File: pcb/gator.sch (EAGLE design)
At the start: 89 parts, among them J2 POWER_JACKPTH, X1 USB-A-S, Y1 12MHz

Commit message: Added tons of decoupling capacitors
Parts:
- added C20: 10u, SparkFun-Passives:CAP0603-CAP
- added C23, C32, C33, C34, C35, C36, C37, C38, C39, C40, C41, C42, C43, C44: 100n, SparkFun-Passives:CAP0603-CAP
- added U$4: GATOR_HEAD, gator:GATOR_HEAD
- C13, C16, C30, C4, C9: value 2.2u -> 10u
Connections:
- net +3V3: now also C20.2, C41.1, C42.1, C43.1, C44.1
- net GND: now also C20.1, C23.2, C32.2, C33.2, C34.2, C35.2, C36.2, C37.2, C38.2, C39.2, C40.2, C41.2, C42.2, C43.2, C44.2, U$4.L, U$4.R
- net VCCINT: now also C23.1, C32.1, C40.1
- net VCCIO: now also C33.1, C34.1, C35.1, C36.1, C37.1, C38.1, C39.1
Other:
- moved on the sheet: C12, C13, C15, C16, C17, C8, C9, NCP565ST12T3G

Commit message: Added Fusion DRC and CAM settings; added SD SCLK pulldown; added large power supply caps
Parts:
- added C45, C46, C47, C48: 100u, SparkFun-Passives:CAP_POLPTH1
- added C49: 100n, SparkFun-Passives:CAP0603-CAP
- added R38: 10K, SparkFun-Passives:RESISTOR0603-RES
- C6: value 2.2u -> 10u
- R14, R15: value 110 -> 120
- R19: value 5K6 -> 4K7
- R20: value 10K -> 4K7
- R29: value 50 -> 51
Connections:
- net +3V3: now also C45.+
- net GND: now also C45.-, C46.-, C47.-, C48.-, C49.2, R38.1
- net HDMI_DETECT: now also C49.1
- net SD_CLK: now also R38.2
- net V+: now also C47.+, C48.+
- net VCCINT: now also C46.+
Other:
- note added: "Place C20 near SD socket to minimize hotplug ripple"
- moved on the sheet: C20
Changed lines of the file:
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@@
 <part name="P+1" library="supply1" deviceset="V+" device=""/>
 <part name="SUPPLY8" library="supply2" deviceset="GND" device=""/>
-<part name="C6" library="SparkFun-Passives" deviceset="CAP" device="0603-CAP" value="2.2u"/>
+<part name="C6" library="SparkFun-Passives" deviceset="CAP" device="0603-CAP" value="10u"/>
 <part name="P+4" library="supply1" deviceset="V+" device=""/>
 <part name="D1" library="SparkFun-DiscreteSemi" deviceset="DIODE" device="PTH" value="RPROT"/>
@@
 <part name="+3V8" library="supply1" deviceset="+3V3" device=""/>
 <part name="+3V9" library="supply1" deviceset="+3V3" device=""/>
-<part name="R14" library="SparkFun-Passives" deviceset="RESISTOR" device="0603-RES" value="110"/>
-<part name="R15" library="SparkFun-Passives" deviceset="RESISTOR" device="0603-RES" value="110"/>
+<part name="R14" library="SparkFun-Passives" deviceset="RESISTOR" device="0603-RES" value="120"/>
+<part name="R15" library="SparkFun-Passives" deviceset="RESISTOR" device="0603-RES" value="120"/>
 <part name="+3V10" library="supply1" deviceset="+3V3" device=""/>
 <part name="C21" library="SparkFun-Passives" deviceset="CAP" device="0603-CAP" value="10u"/>
@@
 <part name="P+12" library="supply1" deviceset="V+" device=""/>
 <part name="SUPPLY24" library="supply2" deviceset="GND" device=""/>
-<part name="R19" library="SparkFun-Passives" deviceset="RESISTOR" device="0603-RES" value="5K6"/>
-<part name="R20" library="SparkFun-Passives" deviceset="RESISTOR" device="0603-RES" value="10K"/>
+<part name="R19" library="SparkFun-Passives" deviceset="RESISTOR" device="0603-RES" value="4K7"/>
+<part name="R20" library="SparkFun-Passives" deviceset="RESISTOR" device="0603-RES" value="4K7"/>
 <part name="U$2" library="gator" deviceset="HDMI_A" device=""/>
 <part name="SDRAM" library="gator" deviceset="MT48LC16M16A2P" device=""/>
@@
 <part name="X1" library="SparkFun-Connectors" deviceset="USB" device="-A-S"/>
 <part name="VCC11" library="supply1" deviceset="VCCIO" device=""/>
-<part name="R29" library="SparkFun-Passives" deviceset="RESISTOR" device="0603-RES" value="50"/>
+<part name="R29" library="SparkFun-Passives" deviceset="RESISTOR" device="0603-RES" value="51"/>
 <part name="R30" library="SparkFun-Passives" deviceset="RESISTOR" device="0603-RES" value="4K7"/>
 <part name="R31" library="SparkFun-Passives" deviceset="RESISTOR" device="0603-RES" value="4K7"/>
@@
 <part name="C43" library="SparkFun-Passives" deviceset="CAP" device="0603-CAP" value="100n"/>
 <part name="C44" library="SparkFun-Passives" deviceset="CAP" device="0603-CAP" value="100n"/>
+<part name="C45" library="SparkFun-Passives" deviceset="CAP_POL" device="PTH1" value="100u"/>
+<part name="C46" library="SparkFun-Passives" deviceset="CAP_POL" device="PTH1" value="100u"/>
+<part name="C47" library="SparkFun-Passives" deviceset="CAP_POL" device="PTH1" value="100u"/>
+<part name="C48" library="SparkFun-Passives" deviceset="CAP_POL" device="PTH1" value="100u"/>
+<part name="C49" library="SparkFun-Passives" deviceset="CAP" device="0603-CAP" value="100n"/>
+<part name="R38" library="SparkFun-Passives" deviceset="RESISTOR" device="0603-RES" value="10K"/>
 </parts>
 <sheets>
@@
 <plain>
 <text x="-322.58" y="116.84" size="1.778" layer="91">PLL: M=6, N=168, P=2, Q=7</text>
+<text x="-398.78" y="327.66" size="1.778" layer="91">Place C20 near SD socket
+to minimize hotplug ripple</text>
 </plain>
 <instances>
@@
 <instance part="SUPPLY31" gate="GND" x="-261.62" y="383.54"/>
 <instance part="SUPPLY32" gate="GND" x="-276.86" y="383.54"/>
-<instance part="C20" gate="G$1" x="-370.84" y="322.58" rot="R180"/>
+<instance part="C20" gate="G$1" x="-378.46" y="322.58" rot="R180"/>
 <instance part="C23" gate="G$1" x="33.02" y="431.8"/>
 <instance part="C32" gate="G$1" x="43.18" y="431.8"/>
@@
 <instance part="C43" gate="G$1" x="-101.6" y="386.08"/>
 <instance part="C44" gate="G$1" x="-93.98" y="386.08"/>
+<instance part="C45" gate="G$1" x="-83.82" y="388.62"/>
+<instance part="C46" gate="G$1" x="63.5" y="434.34"/>
+<instance part="C47" gate="G$1" x="-309.88" y="393.7"/>
+<instance part="C48" gate="G$1" x="-299.72" y="393.7"/>
+<instance part="C49" gate="G$1" x="-132.08" y="38.1"/>
+<instance part="R38" gate="G$1" x="-370.84" y="309.88" rot="R90"/>
 </instances>
 <busses>
@@
 <junction x="-363.22" y="304.8"/>
 <pinref part="C20" gate="G$1" pin="1"/>
-<wire x1="-370.84" y1="317.5" x2="-363.22" y2="317.5" width="0.1524" layer="91"/>
+<wire x1="-378.46" y1="317.5" x2="-363.22" y2="317.5" width="0.1524" layer="91"/>
 <junction x="-363.22" y="317.5"/>
+<pinref part="R38" gate="G$1" pin="1"/>
+<wire x1="-370.84" y1="304.8" x2="-363.22" y2="304.8" width="0.1524" layer="91"/>
 </segment>
 <segment>
@@
 <wire x1="-320.04" y1="388.62" x2="-347.98" y2="388.62" width="0.1524" layer="91"/>
 <junction x="-347.98" y="388.62"/>
+<pinref part="C47" gate="G$1" pin="-"/>
+<wire x1="-309.88" y1="388.62" x2="-320.04" y2="388.62" width="0.1524" layer="91"/>
+<junction x="-320.04" y="388.62"/>
+<pinref part="C48" gate="G$1" pin="-"/>
+<wire x1="-299.72" y1="388.62" x2="-309.88" y2="388.62" width="0.1524" layer="91"/>
+<junction x="-309.88" y="388.62"/>
 </segment>
 <segment>
@@
 <wire x1="-93.98" y1="383.54" x2="-101.6" y2="383.54" width="0.1524" layer="91"/>
 <junction x="-101.6" y="383.54"/>
+<pinref part="C45" gate="G$1" pin="-"/>
+<wire x1="-83.82" y1="383.54" x2="-93.98" y2="383.54" width="0.1524" layer="91"/>
+<junction x="-93.98" y="383.54"/>
 </segment>
 <segment>
@@
 <wire x1="53.34" y1="429.26" x2="43.18" y2="429.26" width="0.1524" layer="91"/>
 <junction x="43.18" y="429.26"/>
+<pinref part="C46" gate="G$1" pin="-"/>
+<wire x1="63.5" y1="429.26" x2="53.34" y2="429.26" width="0.1524" layer="91"/>
+<junction x="53.34" y="429.26"/>
 </segment>
 <segment>
@@
 <pinref part="U$2" gate="G$1" pin="TMDS_D1_SHLD"/>
 <pinref part="U$2" gate="G$1" pin="TMDS_D2_SHLD"/>
+<pinref part="C49" gate="G$1" pin="2"/>
+<wire x1="-132.08" y1="35.56" x2="-132.08" y2="33.02" width="0.1524" layer="91"/>
+<wire x1="-132.08" y1="33.02" x2="-121.92" y2="33.02" width="0.1524" layer="91"/>
+<junction x="-121.92" y="33.02"/>
 </segment>
 <segment>
@@
 <wire x1="-363.22" y1="325.12" x2="-363.22" y2="327.66" width="0.1524" layer="91"/>
 <pinref part="C20" gate="G$1" pin="2"/>
-<wire x1="-370.84" y1="325.12" x2="-363.22" y2="325.12" width="0.1524" layer="91"/>
+<wire x1="-378.46" y1="325.12" x2="-363.22" y2="325.12" width="0.1524" layer="91"/>
 <junction x="-363.22" y="325.12"/>
 </segment>
@@
 <wire x1="-101.6" y1="391.16" x2="-93.98" y2="391.16" width="0.1524" layer="91"/>
 <junction x="-101.6" y="391.16"/>
+<pinref part="C45" gate="G$1" pin="+"/>
+<wire x1="-93.98" y1="391.16" x2="-83.82" y2="391.16" width="0.1524" layer="91"/>
+<junction x="-93.98" y="391.16"/>
 </segment>
 <segment>
@@
 <segment>
 <pinref part="MICROSD" gate="G$1" pin="SCK"/>
-<wire x1="-345.44" y1="322.58" x2="-347.98" y2="322.58" width="0.1524" layer="91"/>
 <label x="-355.6" y="322.58" size="1.778" layer="95"/>
+<pinref part="R38" gate="G$1" pin="2"/>
+<wire x1="-345.44" y1="322.58" x2="-370.84" y2="322.58" width="0.1524" layer="91"/>
+<wire x1="-370.84" y1="322.58" x2="-370.84" y2="314.96" width="0.1524" layer="91"/>
 </segment>
 <segment>
@@
 <wire x1="-335.28" y1="396.24" x2="-320.04" y2="396.24" width="0.1524" layer="91"/>
 <junction x="-320.04" y="396.24"/>
+<pinref part="C47" gate="G$1" pin="+"/>
+<wire x1="-320.04" y1="396.24" x2="-309.88" y2="396.24" width="0.1524" layer="91"/>
+<pinref part="C48" gate="G$1" pin="+"/>
+<wire x1="-309.88" y1="396.24" x2="-299.72" y2="396.24" width="0.1524" layer="91"/>
+<junction x="-309.88" y="396.24"/>
 </segment>
 <segment>
@@
 <wire x1="53.34" y1="439.42" x2="53.34" y2="436.88" width="0.1524" layer="91"/>
 <junction x="43.18" y="439.42"/>
+<pinref part="C46" gate="G$1" pin="+"/>
+<wire x1="63.5" y1="436.88" x2="63.5" y2="439.42" width="0.1524" layer="91"/>
+<wire x1="63.5" y1="439.42" x2="53.34" y2="439.42" width="0.1524" layer="91"/>
+<junction x="53.34" y="439.42"/>
 </segment>
 <segment>
@@
 <junction x="-121.92" y="43.18"/>
 <label x="-142.24" y="43.18" size="1.778" layer="95"/>
+<pinref part="C49" gate="G$1" pin="1"/>
 </segment>
 <segment>
@@
 </schematic>
 </drawing>
+<compatibility>
+<note version="6.3" minversion="6.2.2" severity="warning">
+Since Version 6.2.2 text objects can contain more than one line,
+which will not be processed correctly with this version.
+</note>
+</compatibility>
 </eagle>

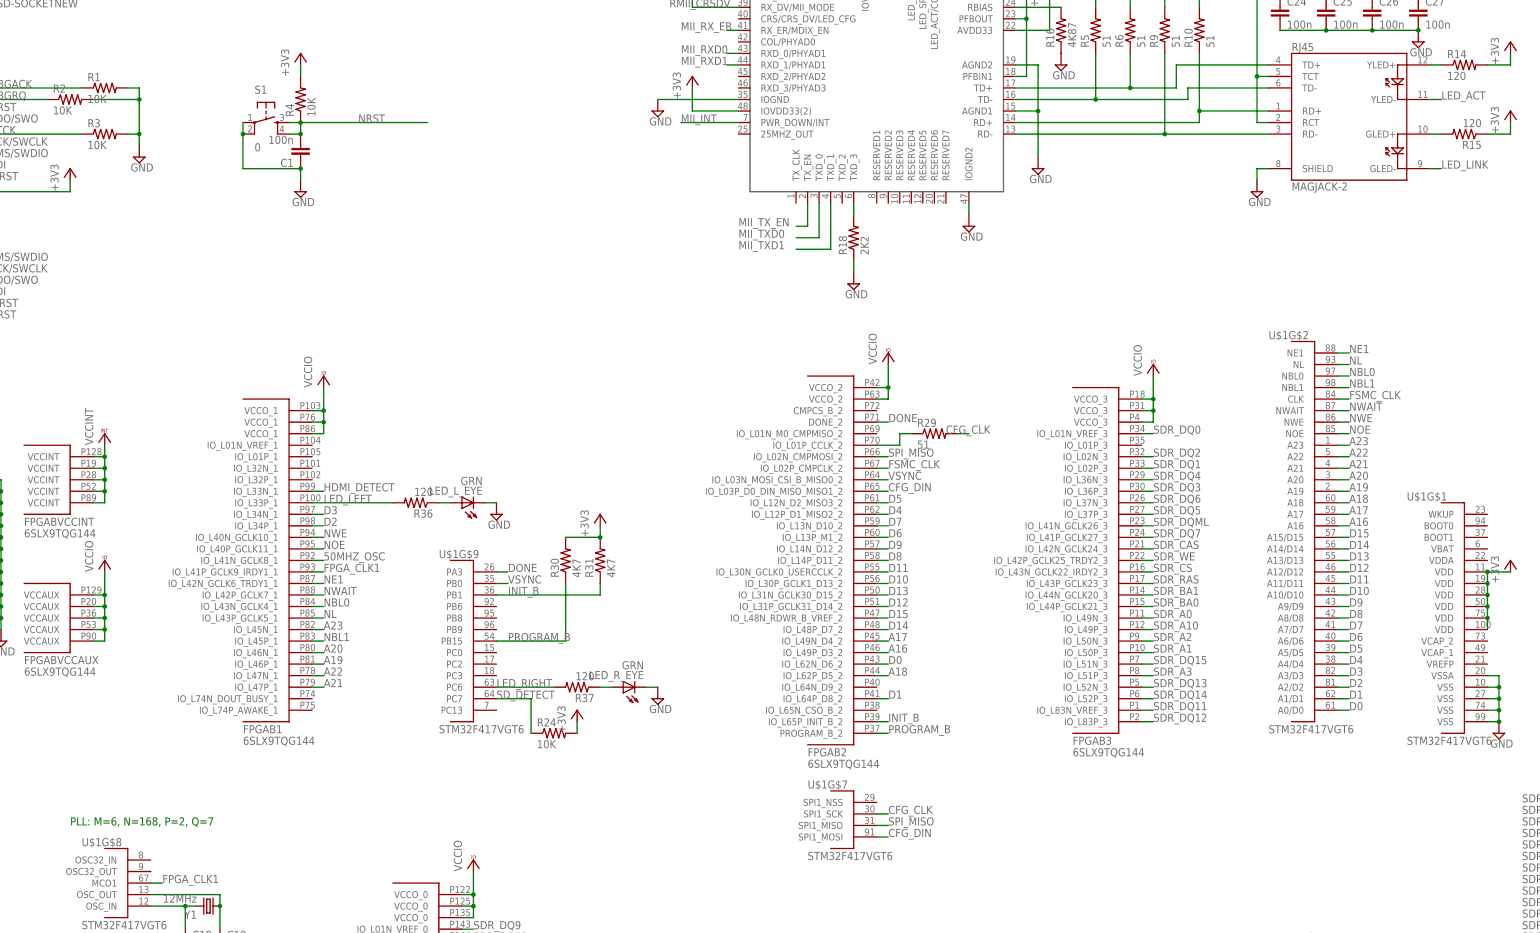
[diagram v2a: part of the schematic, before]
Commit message: Renamed some parts for clarity
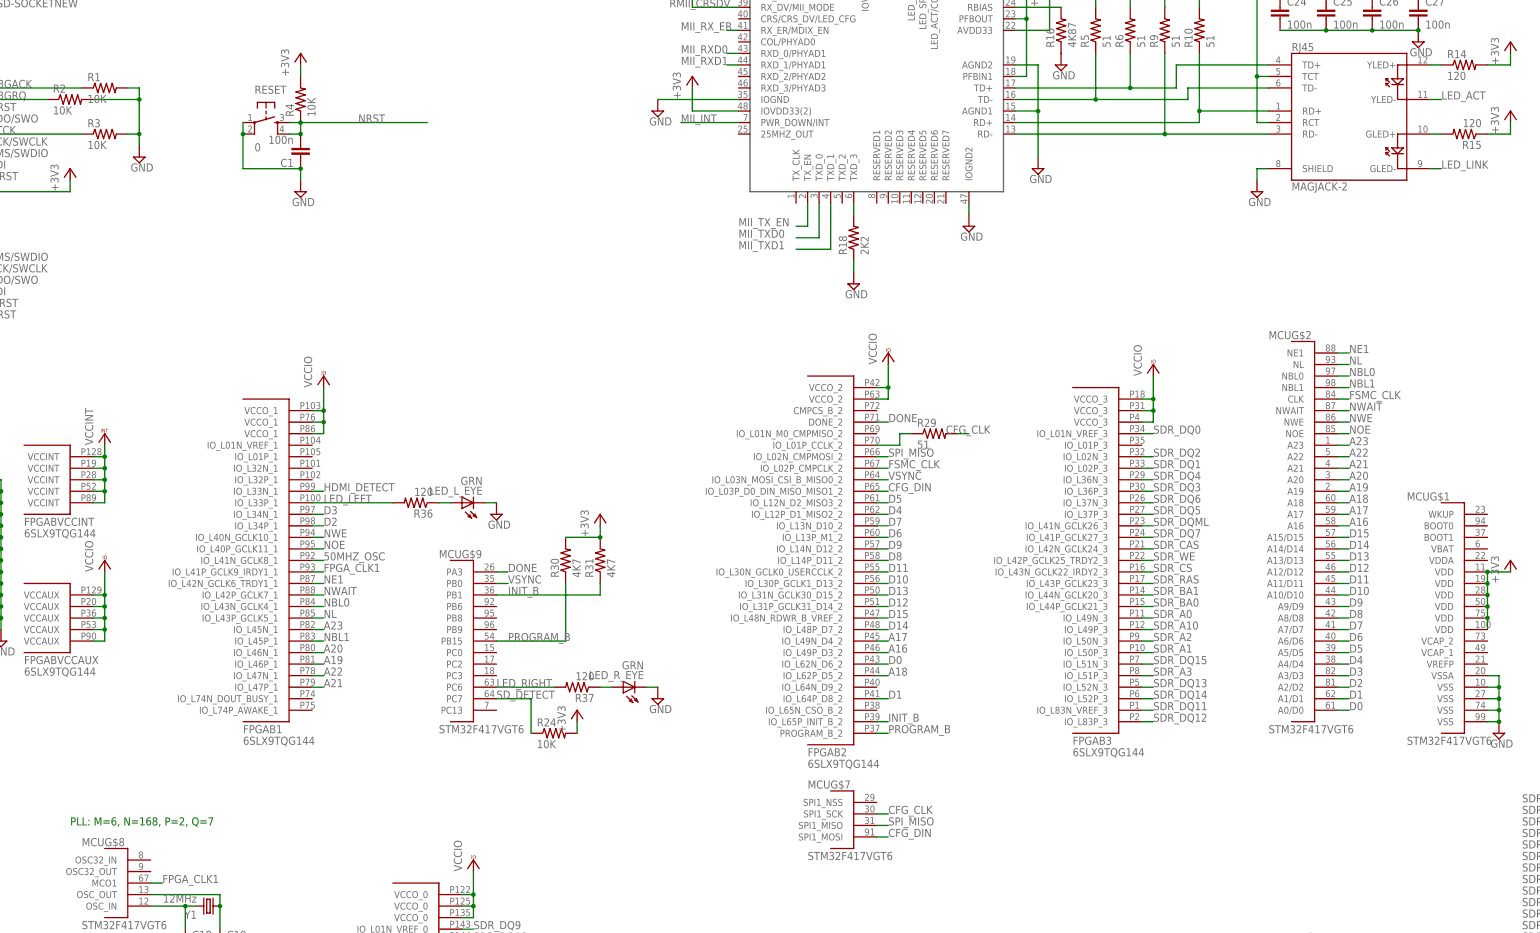
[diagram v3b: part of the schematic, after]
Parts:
- renumbered S1 to RESET, U$1 to MCU

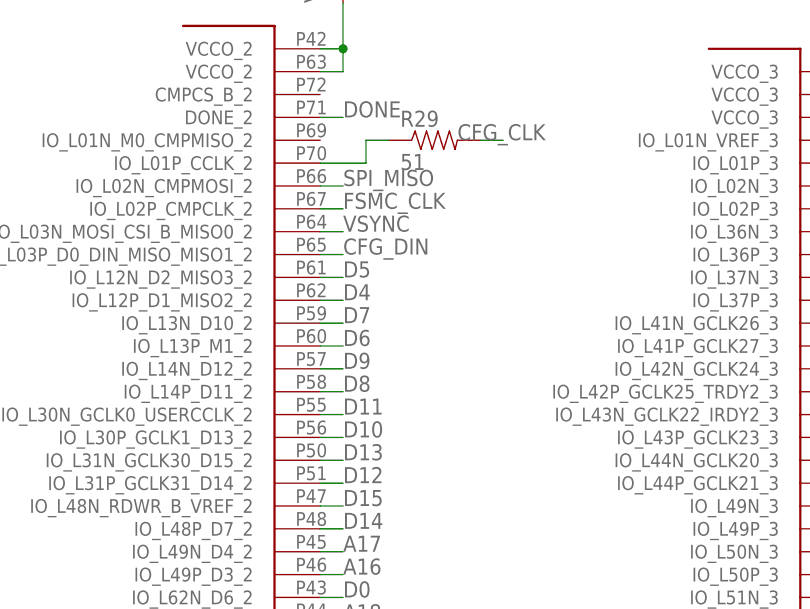
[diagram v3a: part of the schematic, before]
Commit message: Moved FSMC_CLK to a clock input on the FPGA
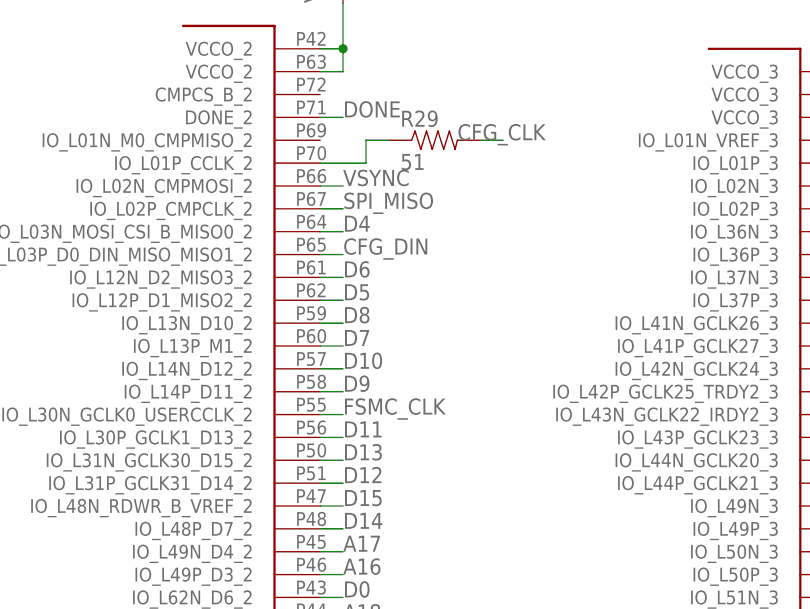
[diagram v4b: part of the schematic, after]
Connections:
- net D10: now also FPGAB2.IO_L14N_D12_2; no longer FPGAB2.IO_L30P_GCLK1_D13_2
- net D11: now also FPGAB2.IO_L30P_GCLK1_D13_2; no longer FPGAB2.IO_L30N_GCLK0_USERCCLK_2
- net D4: now also FPGAB2.IO_L03N_MOSI_CSI_B_MISO0_2; no longer FPGAB2.IO_L12P_D1_MISO2_2
- net D5: now also FPGAB2.IO_L12P_D1_MISO2_2; no longer FPGAB2.IO_L12N_D2_MISO3_2
- net D6: now also FPGAB2.IO_L12N_D2_MISO3_2; no longer FPGAB2.IO_L13P_M1_2
- net D7: now also FPGAB2.IO_L13P_M1_2; no longer FPGAB2.IO_L13N_D10_2
- net D8: now also FPGAB2.IO_L13N_D10_2; no longer FPGAB2.IO_L14P_D11_2
- net D9: now also FPGAB2.IO_L14P_D11_2; no longer FPGAB2.IO_L14N_D12_2
- net FSMC_CLK: now also FPGAB2.IO_L30N_GCLK0_USERCCLK_2; no longer FPGAB2.IO_L02P_CMPCLK_2
- net SPI_MISO: now also FPGAB2.IO_L02P_CMPCLK_2; no longer FPGAB2.IO_L02N_CMPMOSI_2
- net VSYNC: now also FPGAB2.IO_L02N_CMPMOSI_2; no longer FPGAB2.IO_L03N_MOSI_CSI_B_MISO0_2

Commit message: Added pull-ups for sd card and ethernet
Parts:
- added R39, R40, R41, R42, R43: 47K, SparkFun-Passives:RESISTOR0603-RES
- added R44: 1K5, SparkFun-Passives:RESISTOR0603-RES
- R26: value 2K2 -> 10K
- R38: value 10K -> 47K
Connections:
- net +3V3: now also R39.2, R40.2, R41.2, R42.2, R43.2, R44.2
- net MII_MDIO: now also R44.1
- net SD_CMD: now also R41.1
- net SD_D0: now also R42.1
- net SD_D1: now also R43.1
- net SD_D2: now also R39.1
- net SD_D3: now also R40.1
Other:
- note added: "Place caps close to TD, RD, and center taps"
- moved on the sheet: C20, MICROSD, R38
